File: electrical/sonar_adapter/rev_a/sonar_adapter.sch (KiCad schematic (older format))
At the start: 2 parts, among them CN1 SONAR;M1x4RA, CN2 SONAR;F1x4RA

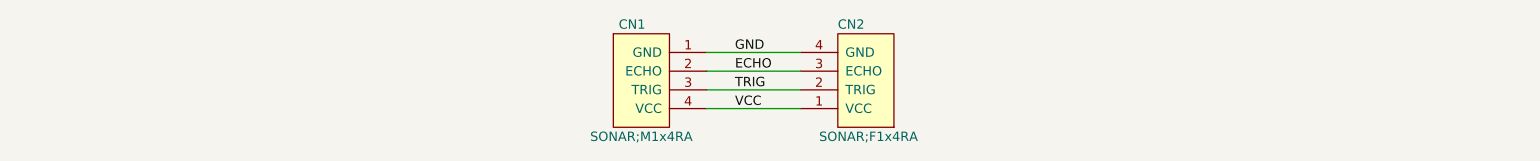
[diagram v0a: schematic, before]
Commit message: Updated Sonar Adapter Rev. A.
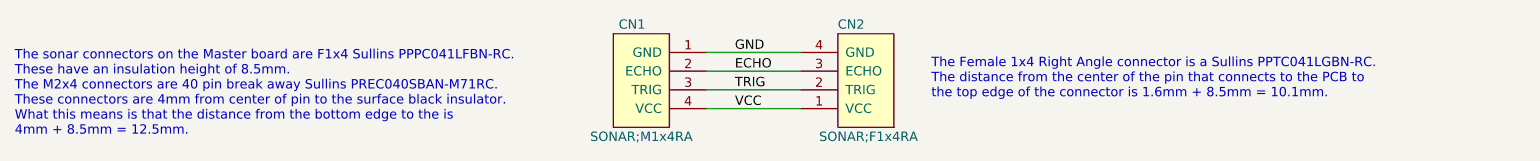
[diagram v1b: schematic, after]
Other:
- note added: "The Female 1x4 Right Angle connector is a Sullins PPTC041LGBN-RC.\nThe distance from the center of the pin that connects to the PCB to\nthe top edge of the connector is 1.6mm + 8.5mm = 10.1mm."
- note added: "The sonar connectors on the Master board are F1x4 Sullins PPPC041LFBN-RC.\nThese have an insulation height of 8.5mm.\nThe M2x4 connectors are 40 pin break away Sullins PREC040SBAN-M71RC.\nThese connectors are 4mm from center of pin to the surface black insulator.\nWhat this means is that the distance from the bottom edge to the is\n4mm + 8.5mm = 12.5mm."
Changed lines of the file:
@@
 Text Label 5150 3800 0    50   ~ 0
 VCC
+Text Notes 6200 3750 0    50   ~ 0
+The Female 1x4 Right Angle connector is a Sullins PPTC041LGBN-RC.\nThe distance from the center of the pin that connects to the PCB to\nthe top edge of the connector is 1.6mm + 8.5mm = 10.1mm.
+Text Notes 1300 3950 0    50   ~ 0
+The sonar connectors on the Master board are F1x4 Sullins PPPC041LFBN-RC.\nThese have an insulation height of 8.5mm.\nThe M2x4 connectors are 40 pin break away Sullins PREC040SBAN-M71RC.\nThese connectors are 4mm from center of pin to the surface black insulator.\nWhat this means is that the distance from the bottom edge to the is\n4mm + 8.5mm = 12.5mm.
 $EndSCHEMATC
